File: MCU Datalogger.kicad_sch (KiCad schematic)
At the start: 0 parts

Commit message: Changes location of symbols (arrange).
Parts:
- added BT1: Battery, symbol Device:Battery
- added C1, C2, C3, C4: C, symbol Device:C
- added C5: C_Polarized, symbol Device:C_Polarized
- added D1, D2: LED, symbol Device:LED
- added H1, H2, H3, H4: MountingHole, symbol Mechanical:MountingHole
- added R1, R2, R3, R4, R5, R6, R7: R, symbol Device:R
- added U1: ATMEGA328P-AU, ATMEGA328P-AU:QFP80P900X900X120-32N, symbol ATMEGA:ATMEGA328P-AU
- added U2: DS1337S_, DS1337S_:SOIC127P600X175-8N, symbol DS13375:DS1337S_
- added U3, U4: 24LC1025, symbol Memory_EEPROM:24LC1025
- added Y1, Y2: Crystal, symbol Device:Crystal
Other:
- added sheet Connectors (Connectors.kicad_sch)
- company: (none) -> CRESENCIO, JESIER S.
- title: (none) -> MCU DATALOGGER WITH MEMORY & CLOCK

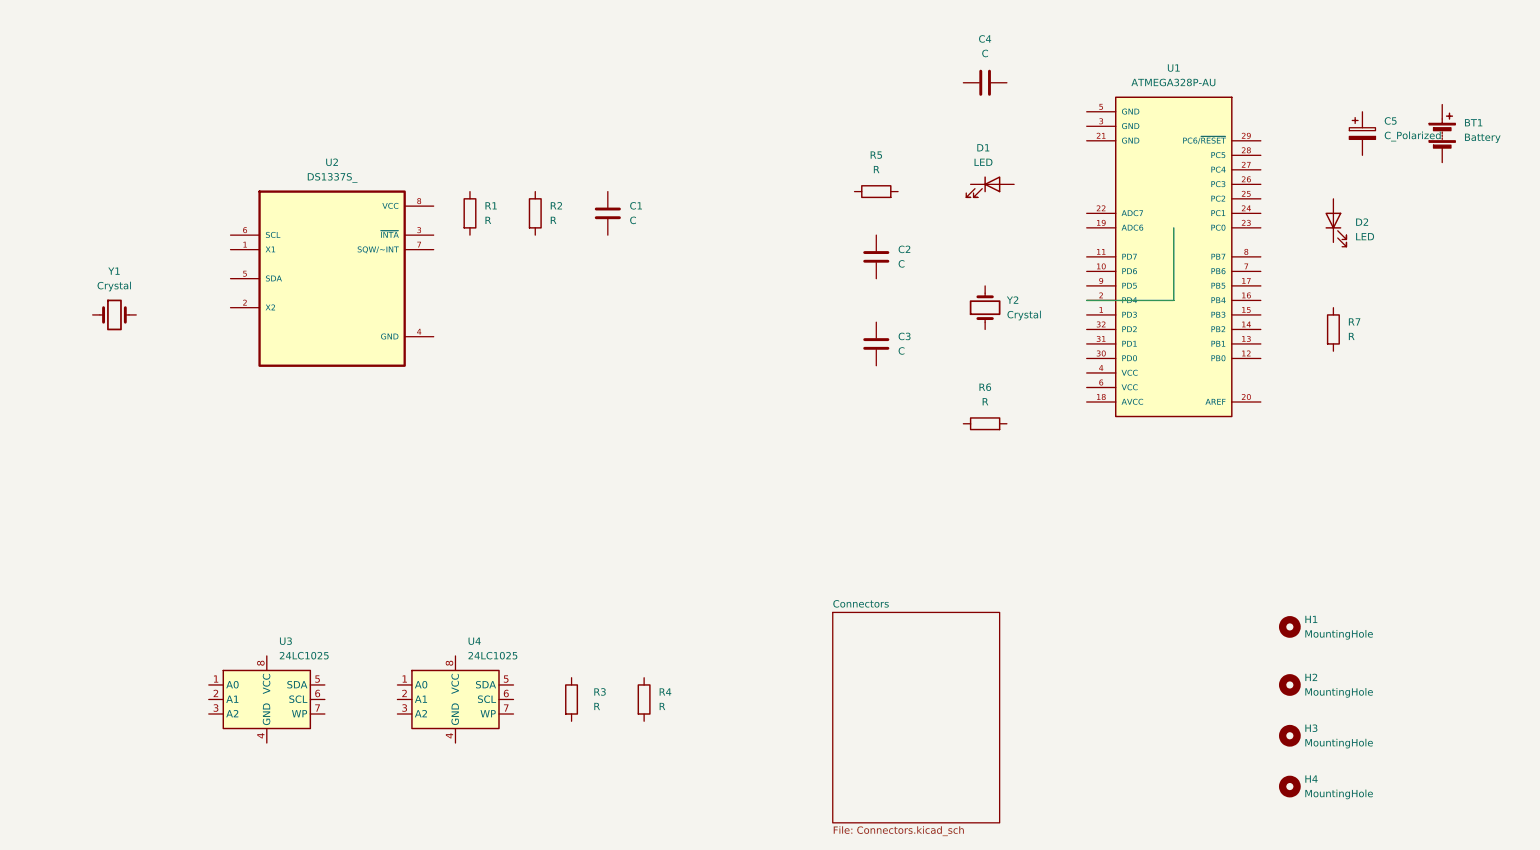
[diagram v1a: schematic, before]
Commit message: Completed wiring of main sheet.
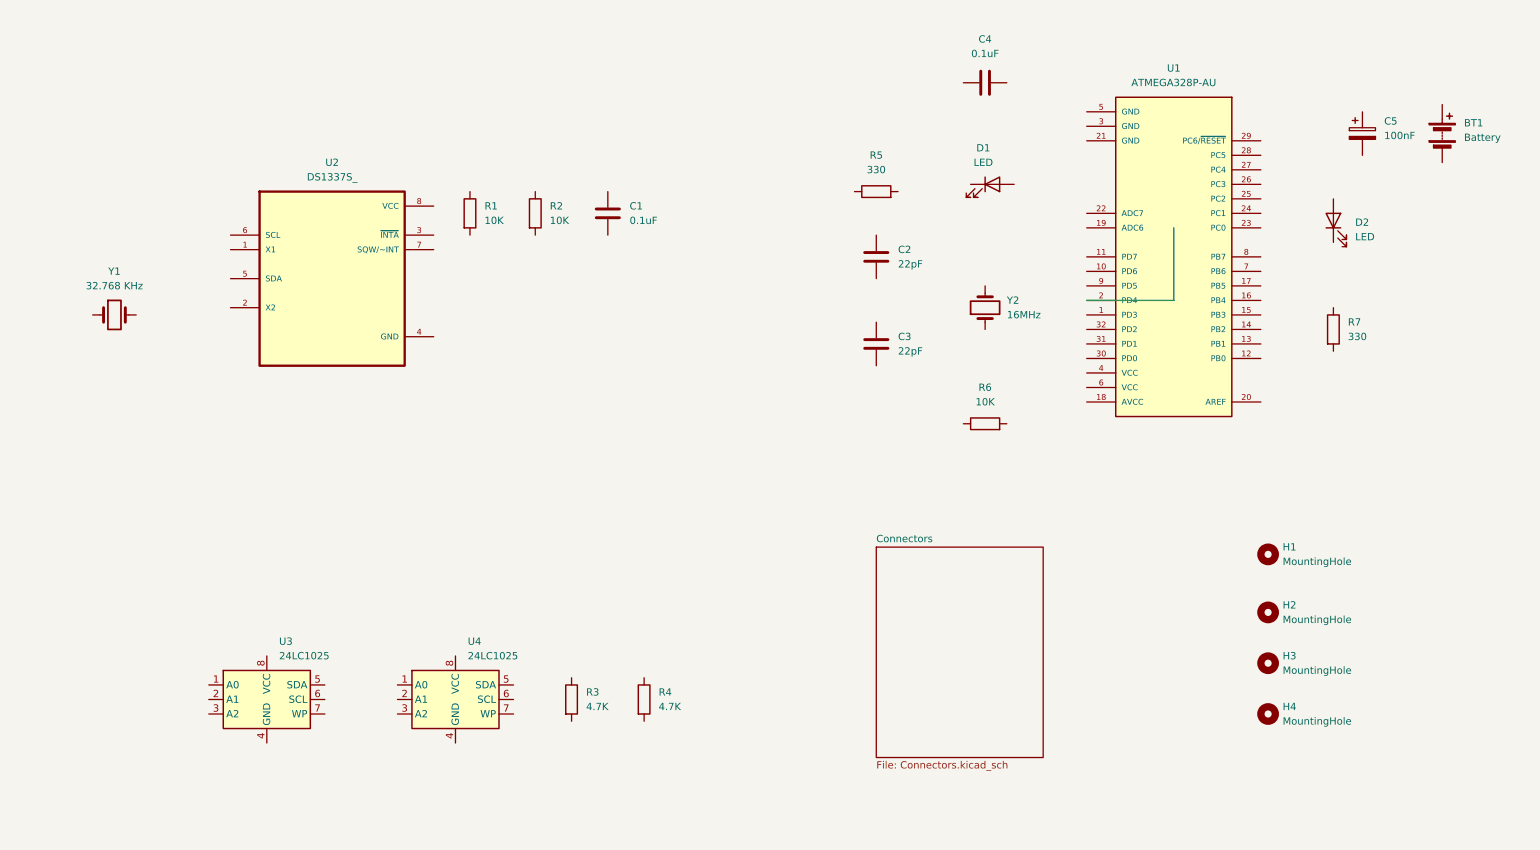
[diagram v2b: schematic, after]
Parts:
- C1, C4: value C -> 0.1uF
- C2, C3: value C -> 22pF
- C5: value C_Polarized -> 100nF
- R1, R2, R6: value R -> 10K
- R3, R4: value R -> 4.7K
- R5, R7: value R -> 330
- Y1: value Crystal -> 32.768 KHz
- Y2: value Crystal -> 16MHz
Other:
- moved on the sheet: H1, H2, H3, H4
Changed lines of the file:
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@@
 			)
 		)
-		(property "Value" "C"
+		(property "Value" "22pF"
 			(at 170.18 63.4999 0)
 			(effects
@@
 			)
 		)
-		(property "Value" "Crystal"
+		(property "Value" "16MHz"
 			(at 189.23 72.3899 90)
 			(effects
@@
 	(symbol
 		(lib_id "Mechanical:MountingHole")
-		(at 238.76 146.05 0)
+		(at 234.95 133.35 0)
 		(unit 1)
 		(exclude_from_sim no)
@@
 		(fields_autoplaced yes)
 		(property "Reference" "H3"
-			(at 241.3 144.7799 0)
+			(at 237.49 132.0799 0)
 			(effects
 				(font
@@
 		)
 		(property "Value" "MountingHole"
-			(at 241.3 147.3199 0)
-			(effects
-				(font
-					(size 1.27 1.27)
-				)
-				(justify left)
-			)
-		)
-		(property "Footprint" ""
-			(at 238.76 146.05 0)
-			(effects
-				(font
-					(size 1.27 1.27)
-				)
-				(hide yes)
-			)
-		)
-		(property "Datasheet" "~"
-			(at 238.76 146.05 0)
+			(at 237.49 134.6199 0)
+			(effects
+				(font
+					(size 1.27 1.27)
+				)
+				(justify left)
+			)
+		)
+		(property "Footprint" ""
+			(at 234.95 133.35 0)
+			(effects
+				(font
+					(size 1.27 1.27)
+				)
+				(hide yes)
+			)
+		)
+		(property "Datasheet" "~"
+			(at 234.95 133.35 0)
 			(effects
 				(font
@@
 		)
 		(property "Description" "Mounting Hole without connection"
-			(at 238.76 146.05 0)
+			(at 234.95 133.35 0)
 			(effects
 				(font
@@
 			)
 		)
-		(property "Value" "R"
+		(property "Value" "10K"
 			(at 97.79 55.8799 0)
 			(effects
@@
 			)
 		)
-		(property "Value" "C"
+		(property "Value" "0.1uF"
 			(at 185.42 26.67 90)
 			(effects
@@
 			)
 		)
-		(property "Value" "R"
+		(property "Value" "330"
 			(at 166.37 46.99 90)
 			(effects
@@
 			)
 		)
-		(property "Value" "C_Polarized"
+		(property "Value" "100nF"
 			(at 255.27 41.0209 0)
 			(effects
@@
 			)
 		)
-		(property "Value" "R"
+		(property "Value" "10K"
 			(at 185.42 87.63 90)
 			(effects
@@
 		(fields_autoplaced yes)
 		(property "Reference" "R3"
-			(at 116.84 138.4299 0)
-			(effects
-				(font
-					(size 1.27 1.27)
-				)
-				(justify left)
-			)
-		)
-		(property "Value" "R"
-			(at 116.84 140.9699 0)
+			(at 115.57 138.4299 0)
+			(effects
+				(font
+					(size 1.27 1.27)
+				)
+				(justify left)
+			)
+		)
+		(property "Value" "4.7K"
+			(at 115.57 140.9699 0)
 			(effects
 				(font
@@
 			)
 		)
-		(property "Value" "R"
+		(property "Value" "4.7K"
 			(at 128.27 140.9699 0)
 			(effects
@@
 	(symbol
 		(lib_id "Mechanical:MountingHole")
-		(at 238.76 154.94 0)
+		(at 234.95 142.24 0)
 		(unit 1)
 		(exclude_from_sim no)
@@
 		(fields_autoplaced yes)
 		(property "Reference" "H4"
-			(at 241.3 153.6699 0)
+			(at 237.49 140.9699 0)
 			(effects
 				(font
@@
 		)
 		(property "Value" "MountingHole"
-			(at 241.3 156.2099 0)
-			(effects
-				(font
-					(size 1.27 1.27)
-				)
-				(justify left)
-			)
-		)
-		(property "Footprint" ""
-			(at 238.76 154.94 0)
-			(effects
-				(font
-					(size 1.27 1.27)
-				)
-				(hide yes)
-			)
-		)
-		(property "Datasheet" "~"
-			(at 238.76 154.94 0)
+			(at 237.49 143.5099 0)
+			(effects
+				(font
+					(size 1.27 1.27)
+				)
+				(justify left)
+			)
+		)
+		(property "Footprint" ""
+			(at 234.95 142.24 0)
+			(effects
+				(font
+					(size 1.27 1.27)
+				)
+				(hide yes)
+			)
+		)
+		(property "Datasheet" "~"
+			(at 234.95 142.24 0)
 			(effects
 				(font
@@
 		)
 		(property "Description" "Mounting Hole without connection"
-			(at 238.76 154.94 0)
+			(at 234.95 142.24 0)
 			(effects
 				(font
@@
 			)
 		)
-		(property "Value" "C"
+		(property "Value" "22pF"
 			(at 170.18 78.7399 0)
 			(effects
@@
 	(symbol
 		(lib_id "Mechanical:MountingHole")
-		(at 238.76 127 0)
+		(at 234.95 114.3 0)
 		(unit 1)
 		(exclude_from_sim no)
@@
 		(fields_autoplaced yes)
 		(property "Reference" "H1"
-			(at 241.3 125.7299 0)
+			(at 237.49 113.0299 0)
 			(effects
 				(font
@@
 		)
 		(property "Value" "MountingHole"
-			(at 241.3 128.2699 0)
-			(effects
-				(font
-					(size 1.27 1.27)
-				)
-				(justify left)
-			)
-		)
-		(property "Footprint" ""
-			(at 238.76 127 0)
-			(effects
-				(font
-					(size 1.27 1.27)
-				)
-				(hide yes)
-			)
-		)
-		(property "Datasheet" "~"
-			(at 238.76 127 0)
+			(at 237.49 115.5699 0)
+			(effects
+				(font
+					(size 1.27 1.27)
+				)
+				(justify left)
+			)
+		)
+		(property "Footprint" ""
+			(at 234.95 114.3 0)
+			(effects
+				(font
+					(size 1.27 1.27)
+				)
+				(hide yes)
+			)
+		)
+		(property "Datasheet" "~"
+			(at 234.95 114.3 0)
 			(effects
 				(font
@@
 		)
 		(property "Description" "Mounting Hole without connection"
-			(at 238.76 127 0)
+			(at 234.95 114.3 0)
 			(effects
 				(font
@@
 			)
 		)
-		(property "Value" "Crystal"
+		(property "Value" "32.768 KHz"
 			(at 33.02 67.31 0)
 			(effects
@@
 			)
 		)
-		(property "Value" "R"
+		(property "Value" "330"
 			(at 248.92 76.1999 0)
 			(effects
@@
 			)
 		)
-		(property "Value" "R"
+		(property "Value" "10K"
 			(at 109.22 55.8799 0)
 			(effects
@@
 			)
 		)
-		(property "Value" "C"
+		(property "Value" "0.1uF"
 			(at 123.19 55.8799 0)
 			(effects
@@
 	(symbol
 		(lib_id "Mechanical:MountingHole")
-		(at 238.76 137.16 0)
+		(at 234.95 124.46 0)
 		(unit 1)
 		(exclude_from_sim no)
@@
 		(fields_autoplaced yes)
 		(property "Reference" "H2"
-			(at 241.3 135.8899 0)
+			(at 237.49 123.1899 0)
 			(effects
 				(font
@@
 		)
 		(property "Value" "MountingHole"
-			(at 241.3 138.4299 0)
-			(effects
-				(font
-					(size 1.27 1.27)
-				)
-				(justify left)
-			)
-		)
-		(property "Footprint" ""
-			(at 238.76 137.16 0)
-			(effects
-				(font
-					(size 1.27 1.27)
-				)
-				(hide yes)
-			)
-		)
-		(property "Datasheet" "~"
-			(at 238.76 137.16 0)
+			(at 237.49 125.7299 0)
+			(effects
+				(font
+					(size 1.27 1.27)
+				)
+				(justify left)
+			)
+		)
+		(property "Footprint" ""
+			(at 234.95 124.46 0)
+			(effects
+				(font
+					(size 1.27 1.27)
+				)
+				(hide yes)
+			)
+		)
+		(property "Datasheet" "~"
+			(at 234.95 124.46 0)
 			(effects
 				(font
@@
 		)
 		(property "Description" "Mounting Hole without connection"
-			(at 238.76 137.16 0)
+			(at 234.95 124.46 0)
 			(effects
 				(font
@@
 	)
 	(sheet
-		(at 158.75 124.46)
+		(at 166.37 113.03)
 		(size 29.21 36.83)
 		(exclude_from_sim no)
@@
 		)
 		(property "Sheetname" "Connectors"
-			(at 158.75 123.7484 0)
+			(at 166.37 112.3184 0)
 			(effects
 				(font
@@
 		)
 		(property "Sheetfile" "Connectors.kicad_sch"
-			(at 158.75 161.8746 0)
-			(effects
-				(font
+			(at 166.37 150.4446 0)
+			(effects
+				(font

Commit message: Completed wiring main sheet.
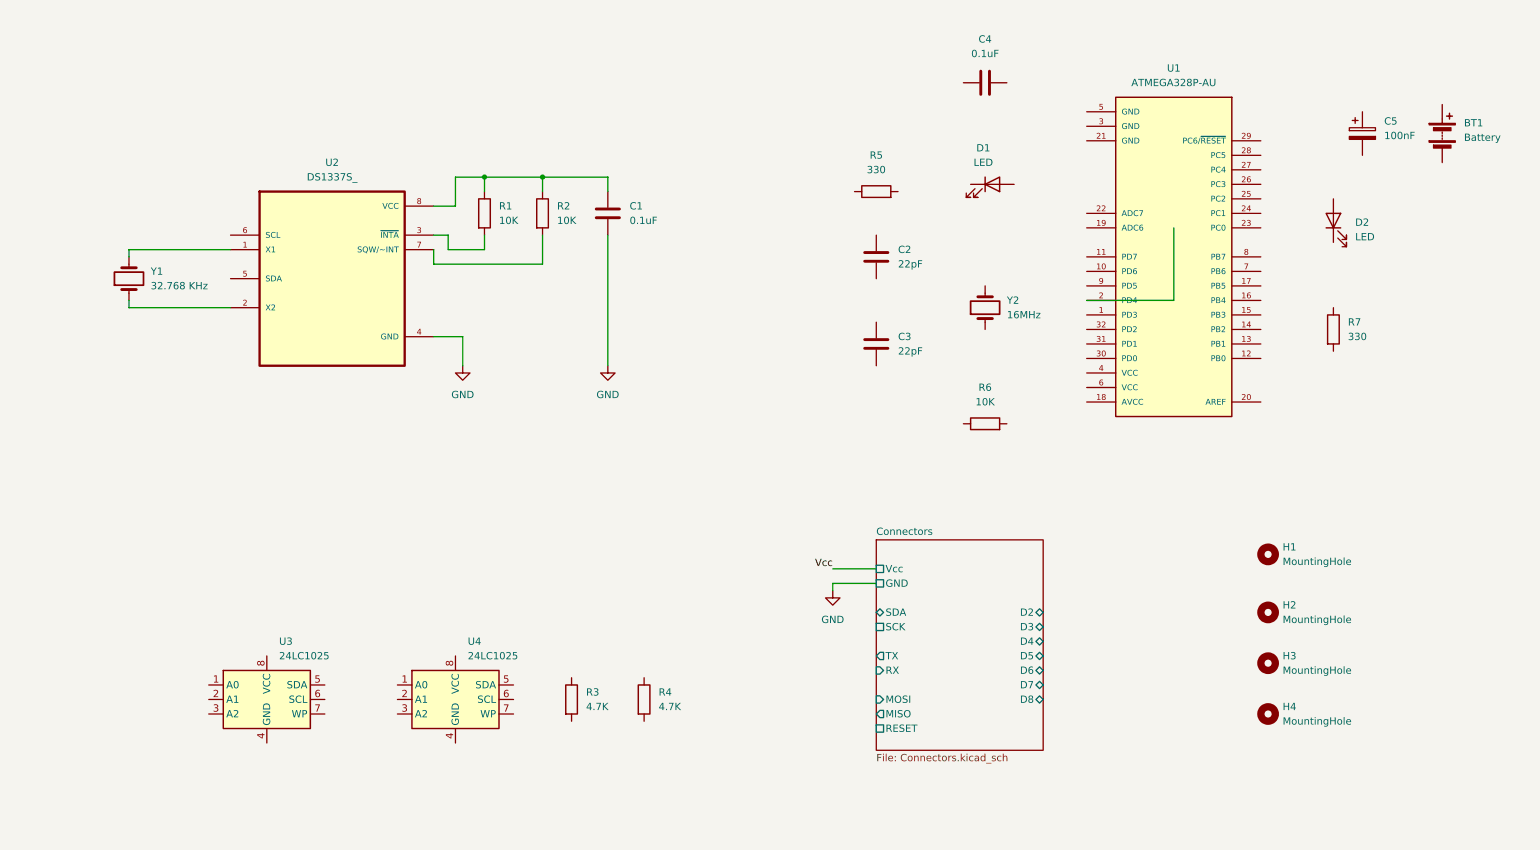
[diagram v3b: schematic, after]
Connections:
- net at R1.1: now also C1.1, R2.1, U2.8 (VCC)
- net at R1.2: now also U2.3 (~{INTA})
- net at U2.1 (X1): now also Y1.2
- net at U2.2 (X2): now also Y1.1
- net GND: now reaches U2.4 (GND)
- net GND: now also C1.2
- net at U2.7 (SQW/~INT): now also R2.2
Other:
- sheet Connectors ports: added D2, D3, D4, D5, D6, D7, D8, GND, MISO, MOSI, RESET, RX, SCK, SDA, TX, Vcc; removed none
- moved on the sheet: R1, R2, Y1

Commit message: Completed comments.
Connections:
- net GND: now also BT1.2 (-), C2.2, C3.2, C4.1, C5.2, R5.1, R7.2, U1.21 (GND), U1.3 (GND), U1.5 (GND), U3.4 (GND), U3.7 (WP), U4.2 (A1), U4.4 (GND), U4.7 (WP)
- net Vcc: now also C1.1, R1.1, R2.1, R3.1, R4.1, R6.1, U2.8 (VCC), U3.1 (A0), U3.2 (A1), U3.3 (A2), U3.8 (VCC), U4.1 (A0), U4.3 (A2), U4.8 (VCC)
- net SDA: now reaches U4.5 (SDA)
- net SDA: now also R4.2, U1.27 (PC4), U2.5 (SDA), U3.5 (SDA)
- net SCK: now reaches U4.6 (SCL)
- net SCK: now also D1.2 (A), R3.2, U1.17 (PB5), U1.28 (PC5), U2.6 (SCL), U3.6 (SCL)
- net at C2.1: now also U1.7 (PB6), Y2.2
- net at D1.1 (K): now also R5.2
- net at Y2.1: now also C3.1, U1.8 (PB7)
- net at C4.2: now also U1.20 (AREF)
- net D3: now reaches U1.1 (PD3)
- net D6: now reaches U1.10 (PD6)
- net D7: now reaches U1.11 (PD7)
- net D8: now reaches U1.12 (PB0)
- net MOSI: now reaches U1.15 (PB3)
- net MISO: now reaches U1.16 (PB4)
- net at U1.18 (AVCC): now also BT1.1 (+), C5.1, D2.2 (A), U1.4 (VCC)
- net D4: now reaches U1.2 (PD4)
- net RESET: now reaches U1.29 (PC6/~{RESET})
- net RESET: now also R6.2
- net RX: now reaches U1.30 (PD0)
- net TX: now reaches U1.31 (PD1)
- net D2: now reaches U1.32 (PD2)
- net D5: now reaches U1.9 (PD5)
- net at D2.1 (K): now also R7.1
- no-connect marks 0 -> 9
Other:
- note added: "EEPROM"
- note added: "MCU"
- note added: "MOUNTING"
- note added: "Real time clock"
- moved on the sheet: BT1, C1, C2, C3, C4, C5, D1, D2, H1, H2, H3, H4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
